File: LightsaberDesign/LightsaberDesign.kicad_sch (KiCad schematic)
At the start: 36 parts, among them M1 Motor_DC, Q1 Q_PMOS_GSD, Q2 Q_NMOS_GSD, Q3 Q_NMOS_GSD, Q4 Q_NMOS_GSD, SW1 SW_Push, U1 LT1377CS8, U2 STM32F446RETx, U3 AP22814AW5

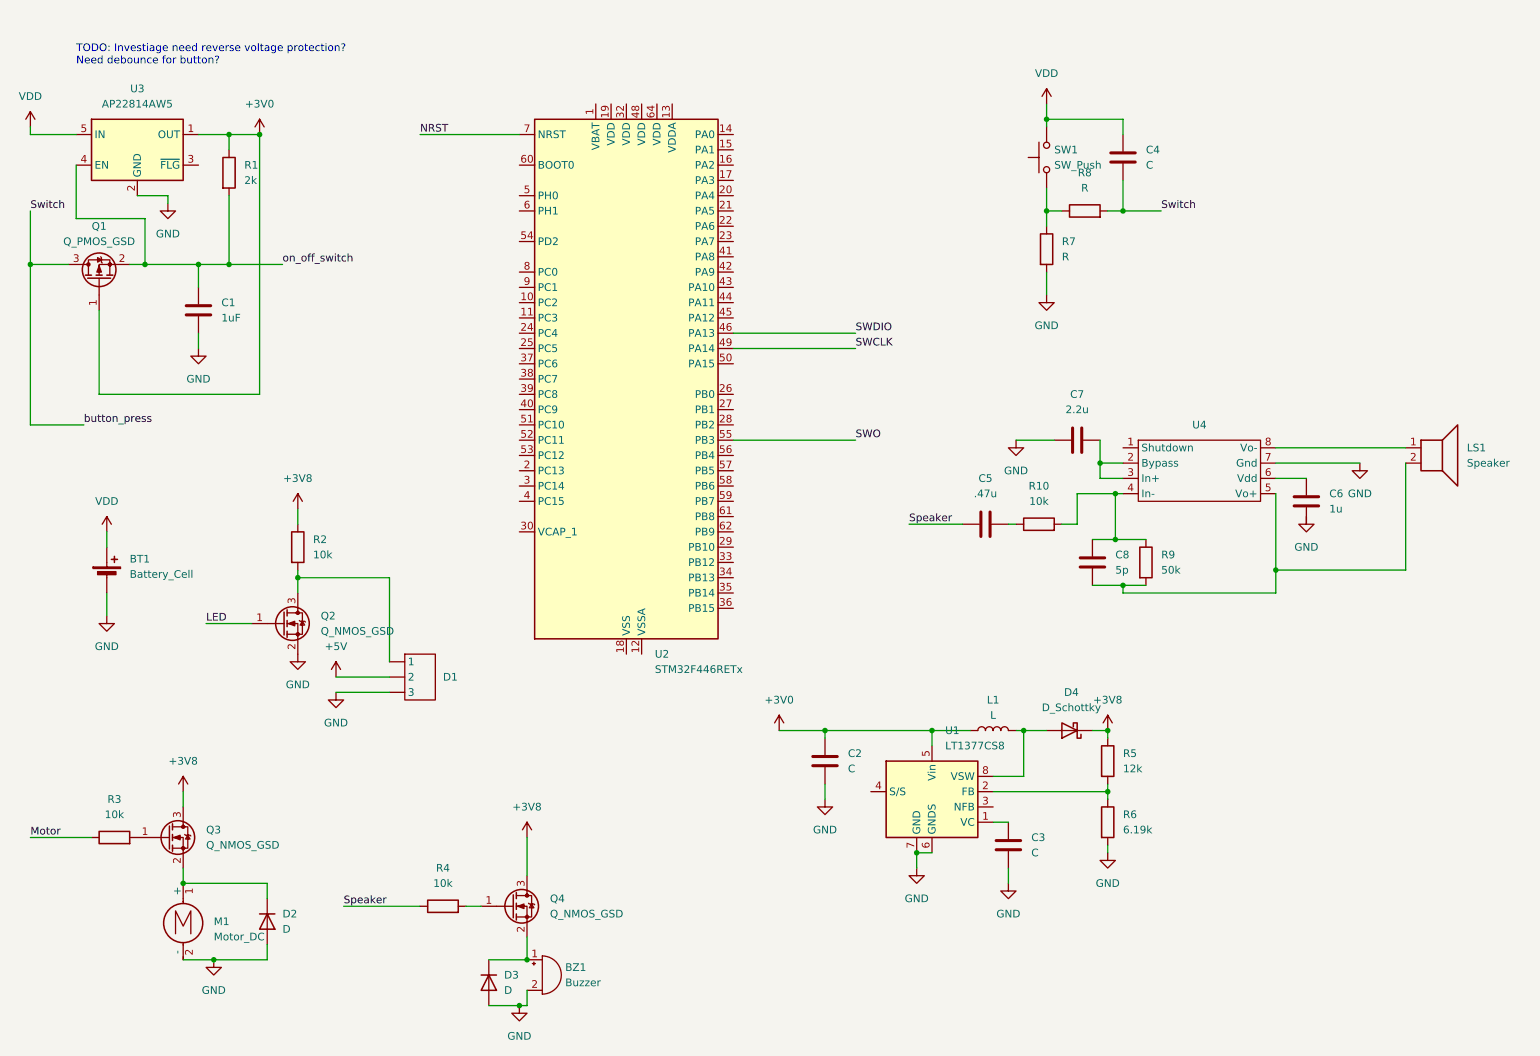
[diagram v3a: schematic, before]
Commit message: Layed out pcb
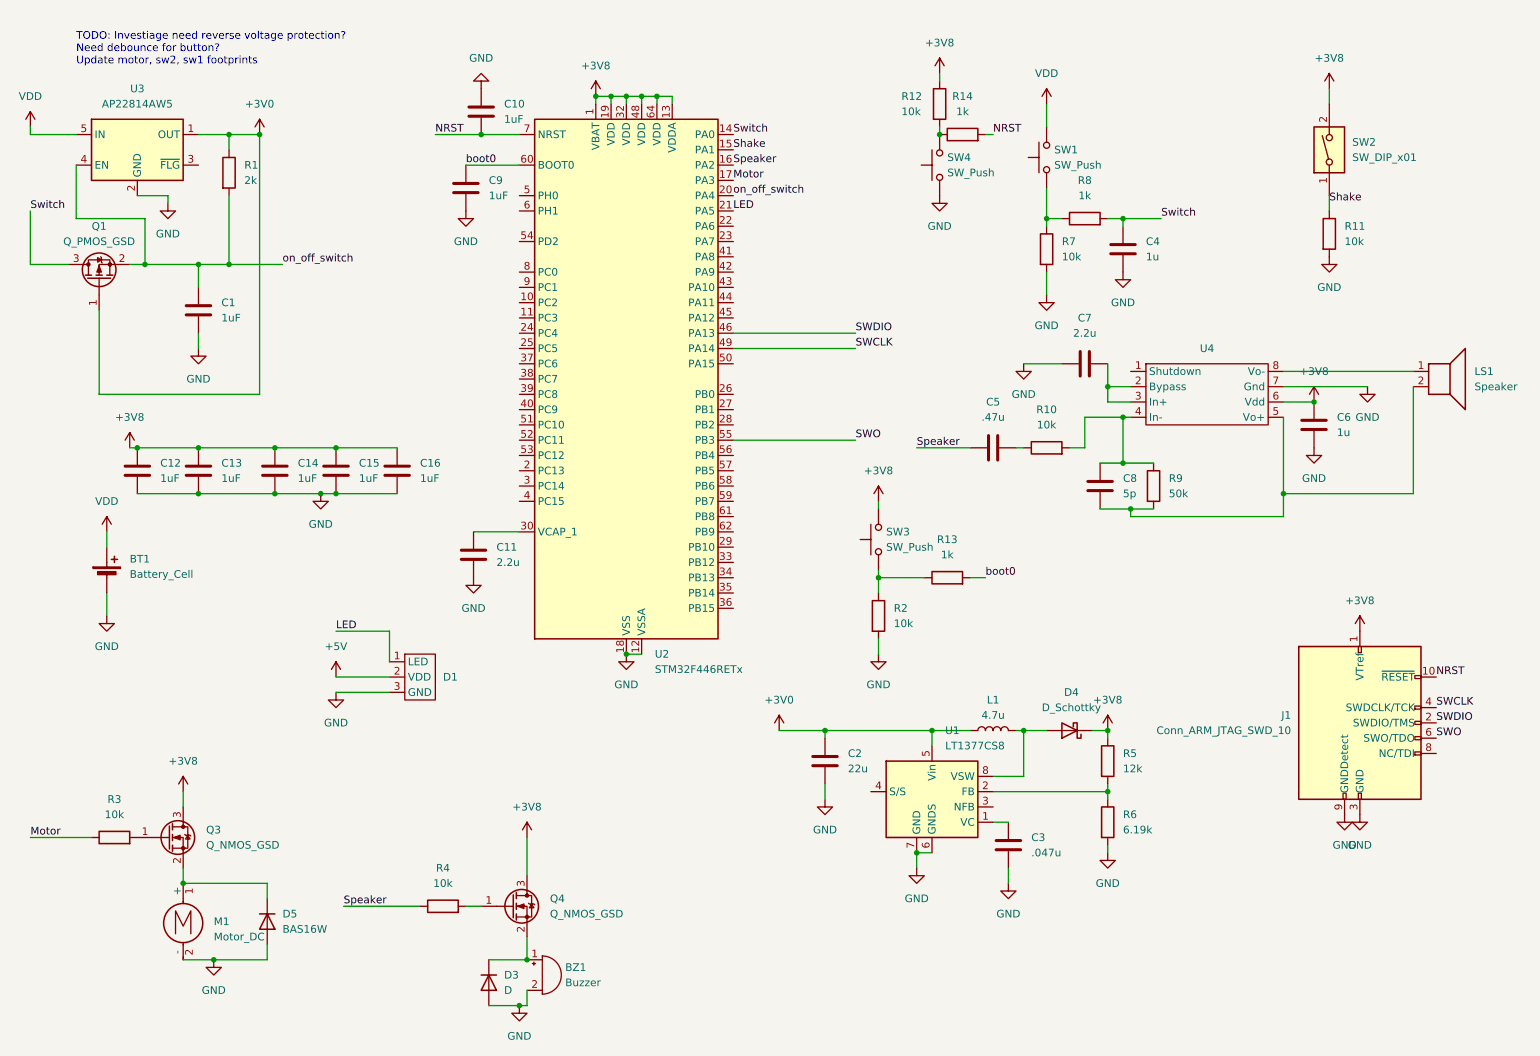
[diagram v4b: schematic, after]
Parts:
- removed D2: D, symbol Device:D
- removed Q2: Q_NMOS_GSD, Package_TO_SOT_SMD:SOT-23-3, symbol Device:Q_NMOS_GSD
- added C10, C12, C13, C14, C15, C16, C9: 1uF, Capacitor_SMD:C_0805_2012Metric_Pad1.18x1.45mm_HandSolder, symbol Device:C
- added C11: 2.2u, Capacitor_SMD:C_0805_2012Metric_Pad1.18x1.45mm_HandSolder, symbol Device:C
- added D5: BAS16W, Package_TO_SOT_SMD:SOT-323_SC-70, symbol Diode:BAS16W
- added J1: Conn_ARM_JTAG_SWD_10, Connector_Samtec_HLE_SMD:Samtec_HLE-105-02-xxx-DV_2x05_P2.54mm_Horizontal, symbol Connector:Conn_ARM_JTAG_SWD_10
- added R11, R12: 10k, Resistor_SMD:R_0805_2012Metric_Pad1.20x1.40mm_HandSolder, symbol Device:R
- added R13, R14: 1k, Resistor_SMD:R_0805_2012Metric_Pad1.20x1.40mm_HandSolder, symbol Device:R
- added SW2: SW_DIP_x01, Connector_PinHeader_2.54mm:PinHeader_1x02_P2.54mm_Vertical, symbol Switch:SW_DIP_x01
- added SW3, SW4: SW_Push, Button_Switch_THT:SW_PUSH_6mm, symbol Switch:SW_Push
- BT1: footprint (none) -> Connector_JST:JST_PH_B2B-PH-K_1x02_P2.00mm_Vertical
- C1, C5, C6, C7, C8: footprint (none) -> Capacitor_SMD:C_0805_2012Metric_Pad1.18x1.45mm_HandSolder
- C2: value C -> 22u; footprint (none) -> Capacitor_SMD:C_0805_2012Metric_Pad1.18x1.45mm_HandSolder
- C3: value C -> .047u; footprint (none) -> Capacitor_SMD:C_0805_2012Metric_Pad1.18x1.45mm_HandSolder
- C4: value C -> 1u; footprint (none) -> Capacitor_SMD:C_0805_2012Metric_Pad1.18x1.45mm_HandSolder
- D4: footprint (none) -> Diode_SMD:D_SOD-323_HandSoldering
- L1: value L -> 4.7u; footprint (none) -> Inductor_SMD:L_0805_2012Metric_Pad1.15x1.40mm_HandSolder
- LS1: footprint (none) -> Connector_Molex:Molex_PicoBlade_53047-0210_1x02_P1.25mm_Vertical
- M1, SW1: footprint (none) -> Connector_PinHeader_2.54mm:PinHeader_1x02_P2.54mm_Vertical
- Q1: footprint (none) -> Package_TO_SOT_SMD:TSOT-23_HandSoldering
- R1, R10, R2, R3, R4, R5, R6, R9: footprint (none) -> Resistor_SMD:R_0805_2012Metric_Pad1.20x1.40mm_HandSolder
- R7: value R -> 10k; footprint (none) -> Resistor_SMD:R_0805_2012Metric_Pad1.20x1.40mm_HandSolder
- R8: value R -> 1k; footprint (none) -> Resistor_SMD:R_0805_2012Metric_Pad1.20x1.40mm_HandSolder
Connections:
- net +3V8: now also C6.1, U2.1 (VBAT), U2.13 (VDDA), U2.19 (VDD), U2.32 (VDD), U2.48 (VDD), U2.64 (VDD), U4.6 (Vdd), C12.1, C13.1, C14.1, C15.1, C16.1, J1.1 (VTref), R12.1, SW2.2, SW3.2; no longer R2.1
- net +5V: now also D1.2 (VDD); no longer D1. (3)
- net GND: now also C4.2, C6.2, D1.3 (GND), R2.2, U2.12 (VSSA), U2.18 (VSS), U2.31 (VSS), U2.47 (VSS), U2.63 (VSS), C10.1, C11.2, C12.2, C13.2, C14.2, C15.2, C16.2, C9.2, D5.1 (A), J1.3 (GND), J1.5 (GND), J1.9 (GNDDetect), R11.2, SW4.1; no longer D1. (3)
- net LED: now also D1.1 (LED), U2.21 (PA5)
- net Motor: now also U2.17 (PA3)
- net NRST: now also C10.2, J1.10 (~{RESET}), R14.2
- net SWCLK: now also J1.4 (SWDCLK/TCK)
- net SWDIO: now also J1.2 (SWDIO/TMS)
- net SWO: now also J1.6 (SWO/TDO)
- net Speaker: now also U2.16 (PA2)
- net Switch: now also C4.1, U2.14 (PA0); no longer C4.2
- net VDD: no longer C4.1
- net on_off_switch: now also U2.20 (PA4)
- net Shake: now reaches U2.15 (PA1)
- net Shake: now also R11.1, SW2.1
- net at U2.30 (VCAP_1): now also C11.1
- net boot0: now reaches U2.60 (BOOT0)
- net boot0: now also C9.1, R13.2
- net at M1.1 (+), Q3.2 (S): now also D5.3 (K)
- new net: R12.2, R14.1, SW4.2
- new net: R13.1, R2.1, SW3.1
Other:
- note added: "TODO: Investiage need reverse voltage protection? Need debounce for button? Update motor, sw2, sw1 footprints"
- note removed: "TODO: Investiage need reverse voltage protection? Need debounce for button?"
- moved on the sheet: C5, C6, C7, C8, LS1, R10, R8, R9, U4

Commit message: Added crystal, ferrite bead
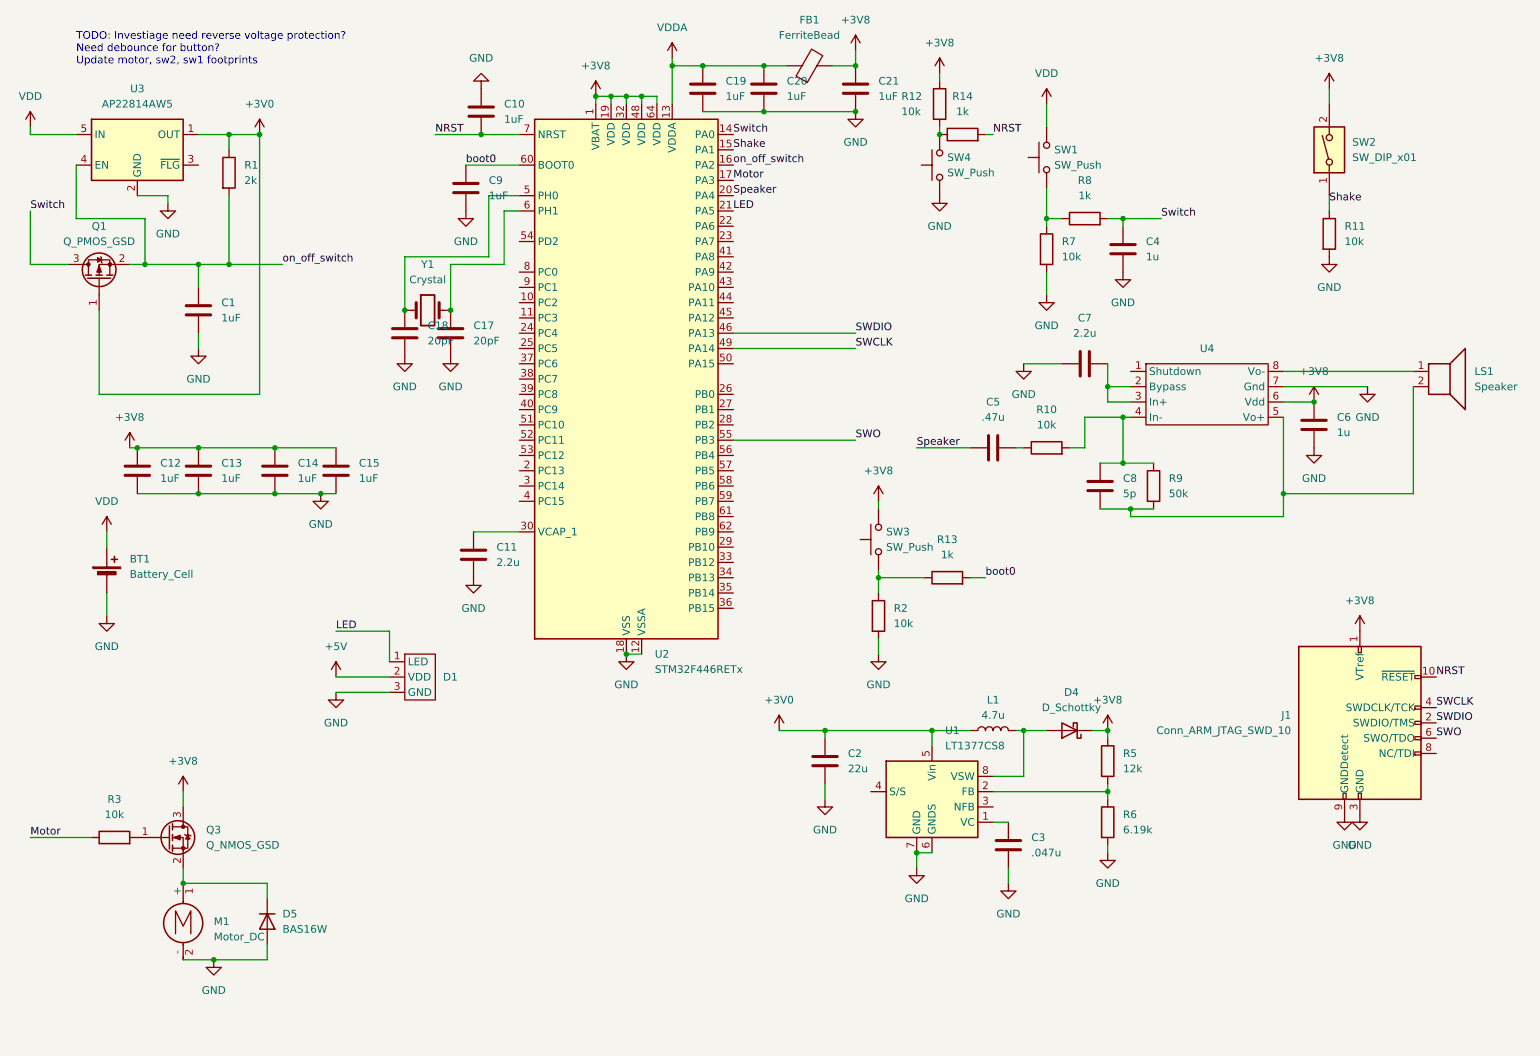
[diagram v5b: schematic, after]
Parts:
- removed BZ1: Buzzer, symbol Device:Buzzer
- removed C16: 1uF, Capacitor_SMD:C_0805_2012Metric_Pad1.18x1.45mm_HandSolder, symbol Device:C
- removed D3: D, symbol Device:D
- removed Q4: Q_NMOS_GSD, Package_TO_SOT_SMD:SOT-23-3, symbol Device:Q_NMOS_GSD
- removed R4: 10k, Resistor_SMD:R_0805_2012Metric_Pad1.20x1.40mm_HandSolder, symbol Device:R
- added C17, C18: 20pF, Capacitor_SMD:C_0805_2012Metric_Pad1.18x1.45mm_HandSolder, symbol Device:C
- added C19, C20, C21: 1uF, Capacitor_SMD:C_0805_2012Metric_Pad1.18x1.45mm_HandSolder, symbol Device:C
- added FB1: FerriteBead, Capacitor_SMD:C_0805_2012Metric_Pad1.18x1.45mm_HandSolder, symbol Device:FerriteBead
- added Y1: Crystal, Crystal:Crystal_SMD_HC49-SD, symbol Device:Crystal
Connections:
- net +3V8: now also C21.1, FB1.2; no longer U2.13 (VDDA)
- net GND: now also C17.2, C18.2, C19.2, C20.2, C21.2
- net Speaker: now also U2.20 (PA4); no longer U2.16 (PA2)
- net on_off_switch: now also U2.16 (PA2); no longer U2.20 (PA4)
- net at U2.5 (PH0): now also C18.1, Y1.1
- net at U2.6 (PH1): now also C17.1, Y1.2
- new net VDDA: C19.1, C20.1, FB1.1, U2.13 (VDDA)

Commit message: Finished drc
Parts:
- M1: footprint Connector_PinHeader_2.54mm:PinHeader_1x02_P2.54mm_Vertical -> Connector_Molex:Molex_PicoBlade_53047-0210_1x02_P1.25mm_Vertical
- SW2: footprint Connector_PinHeader_2.54mm:PinHeader_1x02_P2.54mm_Vertical -> Capacitor_THT:CP_Radial_D4.0mm_P1.50mm
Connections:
- net +5V is gone; now on net +3V8: D1.2 (VDD)
- no-connect marks 0 -> 44

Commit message: Updated capacitor values
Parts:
- C12, C13, C14, C15: value 1uF -> .1uF
- C19: value 1uF -> 10nF
- C4: value 1u -> 1uF
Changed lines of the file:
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@@
       (effects (font (size 1.27 1.27)) (justify left))
     )
-    (property "Value" "1uF" (at 77.47 90.17 0)
+    (property "Value" ".1uF" (at 77.47 90.17 0)
       (effects (font (size 1.27 1.27)) (justify left))
     )
@@
       (effects (font (size 1.27 1.27)) (justify left))
     )
-    (property "Value" "1uF" (at 54.61 90.17 0)
+    (property "Value" ".1uF" (at 54.61 90.17 0)
       (effects (font (size 1.27 1.27)) (justify left))
     )
@@
       (effects (font (size 1.27 1.27)) (justify left))
     )
-    (property "Value" "1u" (at 218.44 53.34 0)
+    (property "Value" "1uF" (at 218.44 53.34 0)
       (effects (font (size 1.27 1.27)) (justify left))
     )
@@
       (effects (font (size 1.27 1.27)) (justify left))
     )
-    (property "Value" "1uF" (at 87.63 90.17 0)
+    (property "Value" ".1uF" (at 87.63 90.17 0)
       (effects (font (size 1.27 1.27)) (justify left))
     )
@@
       (effects (font (size 1.27 1.27)) (justify left))
     )
-    (property "Value" "1uF" (at 148.59 26.67 0)
+    (property "Value" "10nF" (at 148.59 26.67 0)
       (effects (font (size 1.27 1.27)) (justify left))
     )
@@
       (effects (font (size 1.27 1.27)) (justify left))
     )
-    (property "Value" "1uF" (at 64.77 90.17 0)
-      (effects (font (size 1.27 1.27)) (justify left))
-    )
+    (property "Value" ".1uF" (at 64.77 90.17 0)
+      (effects (font (size 1.27 1.27)) (justify left))
+    )

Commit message: Updated PCB with new header
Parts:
- D1: footprint Connector_JST:JST_XH_B3B-XH-A_1x03_P2.50mm_Vertical -> Connector_JST:JST_PH_B3B-PH-K_1x03_P2.00mm_Vertical
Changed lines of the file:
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@@
       (effects (font (size 1.27 1.27)))
     )
-    (property "Footprint" "Connector_JST:JST_XH_B3B-XH-A_1x03_P2.50mm_Vertical" (at 95.25 118.11 0)
+    (property "Footprint" "Connector_JST:JST_PH_B3B-PH-K_1x03_P2.00mm_Vertical" (at 95.25 118.11 0)
       (effects (font (size 1.27 1.27)) hide)
     )
